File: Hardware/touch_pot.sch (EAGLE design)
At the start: 77 parts, among them CON1 SINGLE_PADSMD, CON10 SINGLE_PADSMD, CON11 SINGLE_PADSMD, CON12 SINGLE_PADSMD, CON13 SINGLE_PADSMD, CON14 SINGLE_PADSMD, CON15 SINGLE_PADSMD, CON16 SINGLE_PADSMD_R, CON17 SINGLE_PADSMD_R, CON18 SINGLE_PADSMD_R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

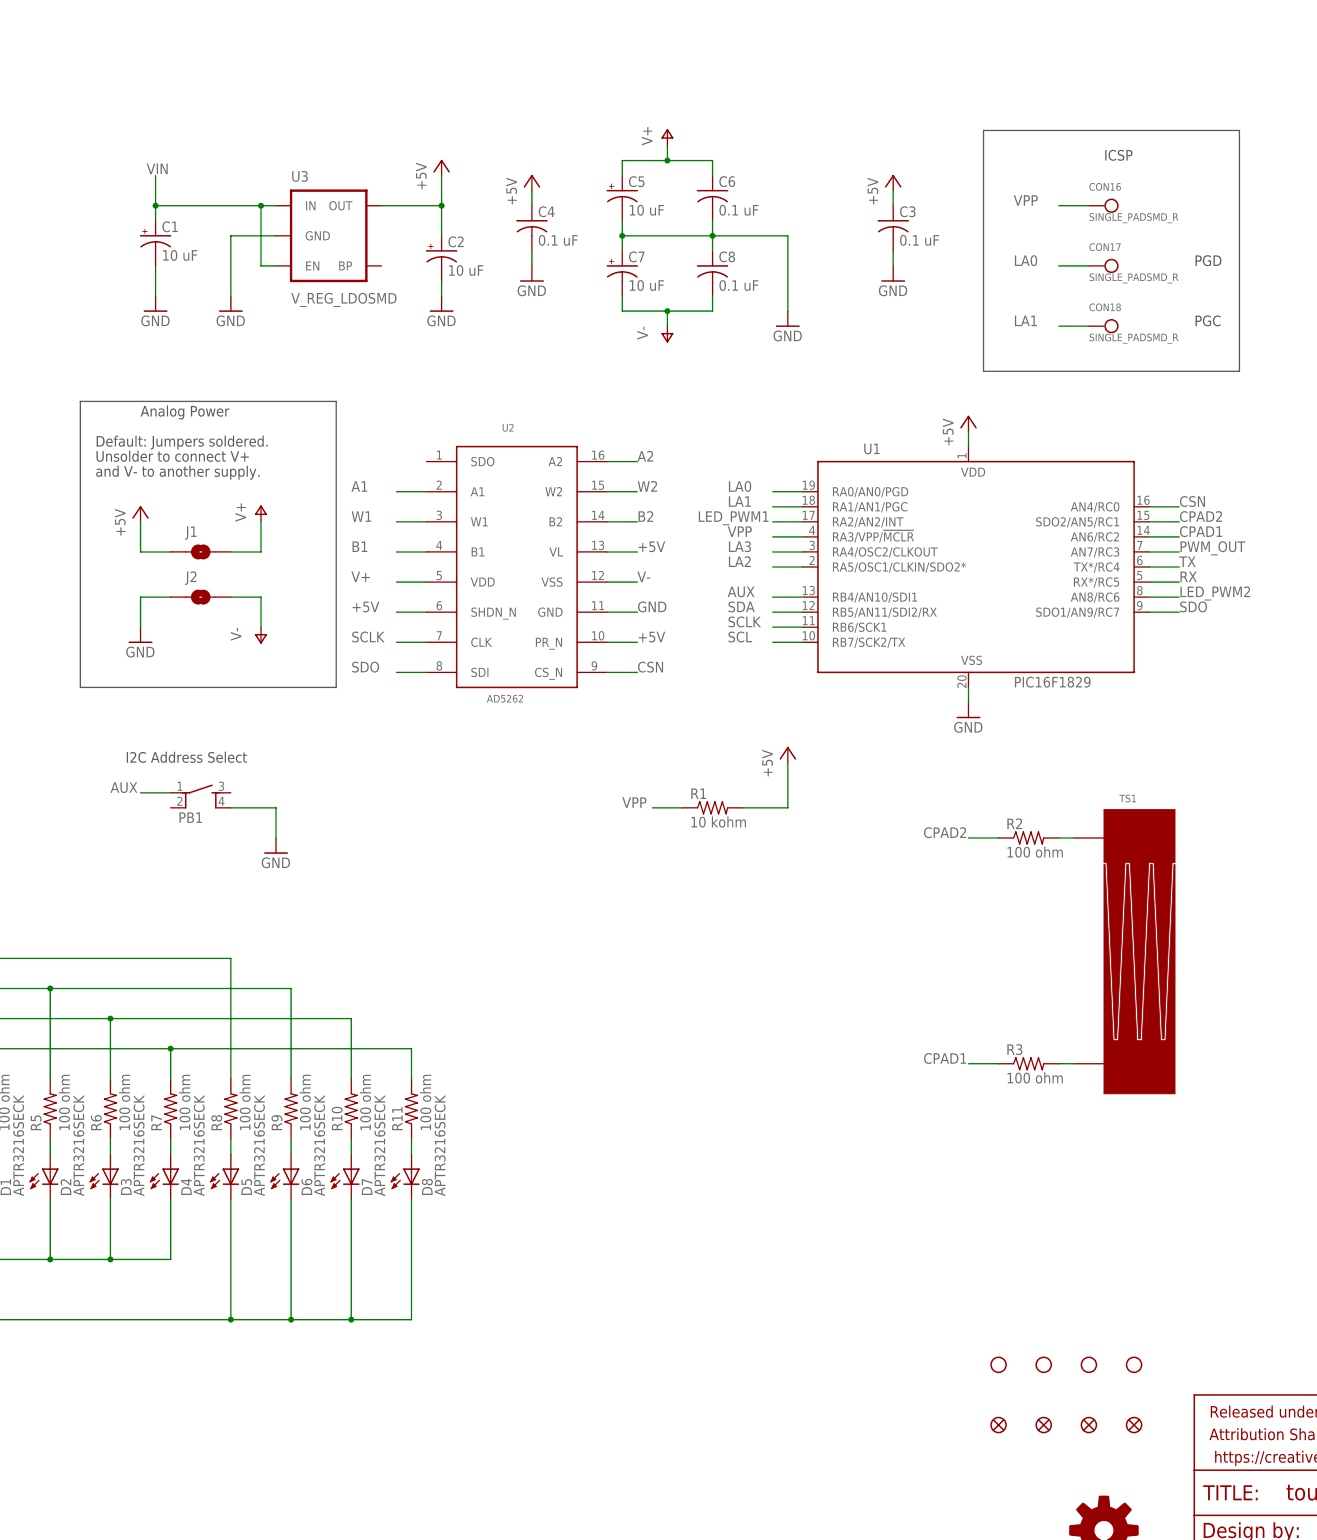
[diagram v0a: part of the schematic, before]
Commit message: 2nd Round of Protos
Added a few test points, moved a cap closer to analog IC, moved button
down to avoid touching resistors.
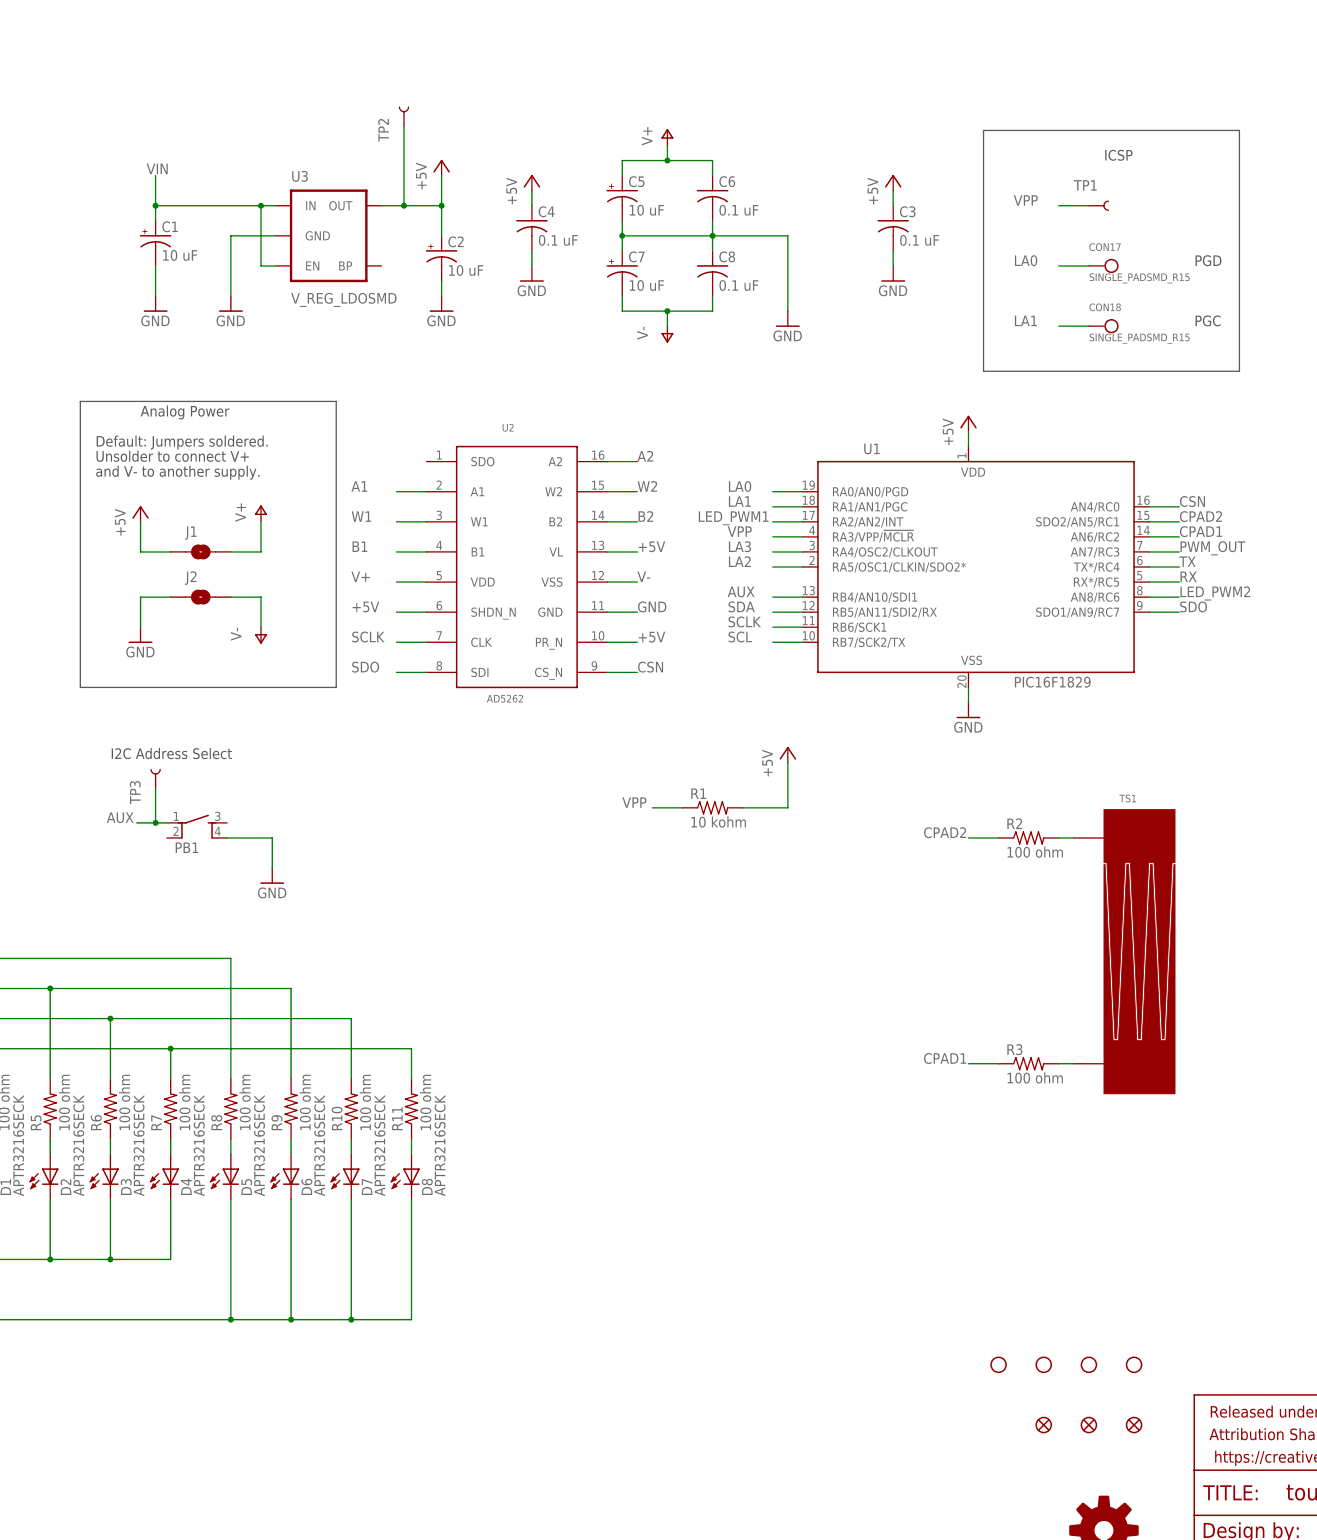
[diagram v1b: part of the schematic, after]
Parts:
- removed CON16: SINGLE_PADSMD_R, djd_eagle_library:SINGLE_PADSMD_R
- removed U$5: FIDUCIAL, djd_eagle_library:FIDUCIAL
- added TP1, TP2, TP3: TEST-POINT3X4, SparkFun-Passives:TEST-POINT3X4
- CON17, CON18: value SINGLE_PADSMD_R -> SINGLE_PADSMD_R15; device djd_eagle_library:SINGLE_PADSMD_R -> djd_eagle_library:SINGLE_PADSMD_R15
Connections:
- net +5V: now also TP2.1
- net AUX: now also TP3.1
- net VPP: now also TP1.1; no longer CON16.P$1
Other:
- moved on the sheet: PB1

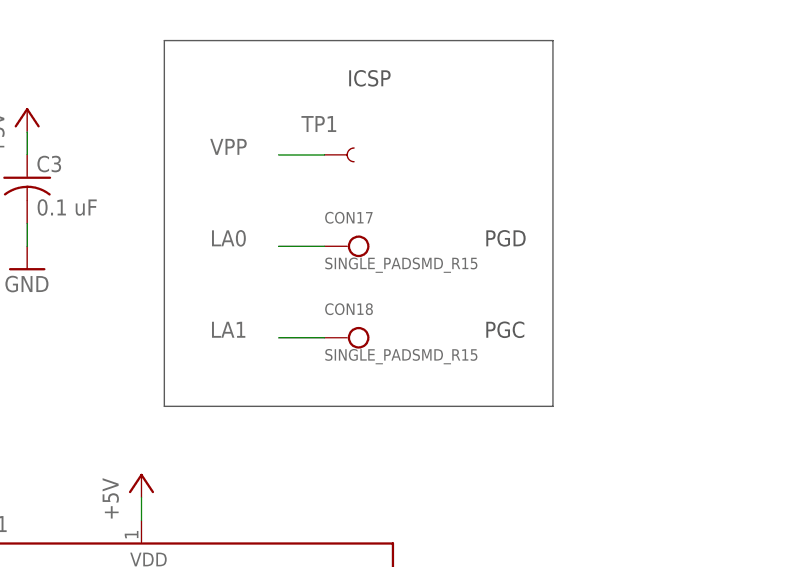
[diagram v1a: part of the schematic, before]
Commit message: Final commit before 2nd round of protos - 4 real
made all test points the same size, trace clean up, moved filtering cap
as close as possible.
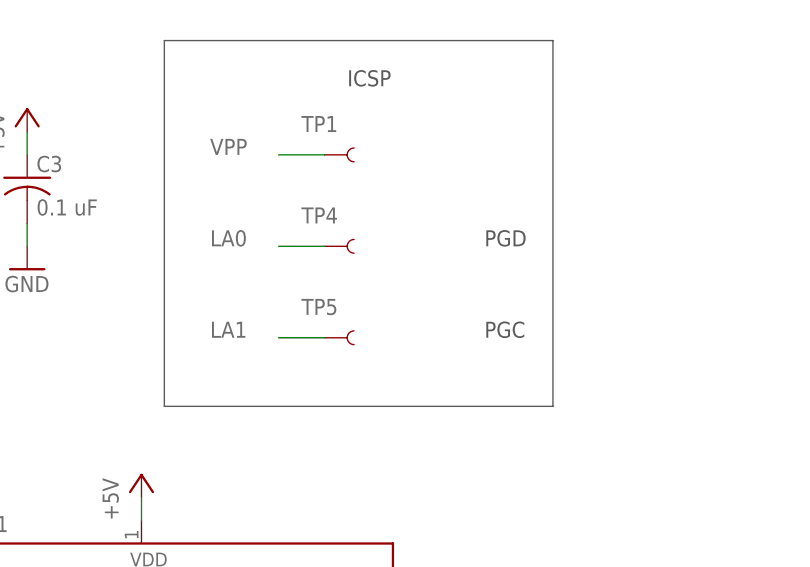
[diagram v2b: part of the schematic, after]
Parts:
- removed CON17, CON18: SINGLE_PADSMD_R15, djd_eagle_library:SINGLE_PADSMD_R15
- added TP4, TP5: TEST-POINT3X4, SparkFun-Passives:TEST-POINT3X4
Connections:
- net LA0: now also TP4.1; no longer CON17.P$1
- net LA1: now also TP5.1; no longer CON18.P$1
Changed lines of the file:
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@@
 <setting verticaltext="up"/>
 </settings>
-<grid distance="0.025" unitdist="inch" unit="inch" style="lines" multiple="1" display="no" altdistance="0.01" altunitdist="inch" altunit="inch"/>
+<grid distance="0.1" unitdist="inch" unit="inch" style="lines" multiple="1" display="no" altdistance="0.01" altunitdist="inch" altunit="inch"/>
 <layers>
-<layer number="1" name="Top" color="4" fill="1" visible="yes" active="no"/>
-<layer number="2" name="Route2" color="1" fill="3" visible="yes" active="no"/>
-<layer number="3" name="Route3" color="4" fill="3" visible="yes" active="no"/>
-<layer number="4" name="Route4" color="1" fill="4" visible="yes" active="no"/>
-<layer number="5" name="Route5" color="4" fill="4" visible="yes" active="no"/>
-<layer number="6" name="Route6" color="1" fill="8" visible="yes" active="no"/>
-<layer number="7" name="Route7" color="4" fill="8" visible="yes" active="no"/>
-<layer number="8" name="Route8" color="1" fill="2" visible="yes" active="no"/>
-<layer number="9" name="Route9" color="4" fill="2" visible="yes" active="no"/>
-<layer number="10" name="Route10" color="1" fill="7" visible="yes" active="no"/>
-<layer number="11" name="Route11" color="4" fill="7" visible="yes" active="no"/>
-<layer number="12" name="Route12" color="1" fill="5" visible="yes" active="no"/>
-<layer number="13" name="Route13" color="4" fill="5" visible="yes" active="no"/>
-<layer number="14" name="Route14" color="1" fill="6" visible="yes" active="no"/>
-<layer number="15" name="Route15" color="4" fill="6" visible="yes" active="no"/>
-<layer number="16" name="Bottom" color="1" fill="1" visible="yes" active="no"/>
-<layer number="17" name="Pads" color="2" fill="1" visible="yes" active="no"/>
-<layer number="18" name="Vias" color="2" fill="1" visible="yes" active="no"/>
-<layer number="19" name="Unrouted" color="6" fill="1" visible="yes" active="no"/>
-<layer number="20" name="Dimension" color="15" fill="1" visible="yes" active="no"/>
-<layer number="21" name="tPlace" color="16" fill="1" visible="yes" active="no"/>
-<layer number="22" name="bPlace" color="14" fill="1" visible="yes" active="no"/>
-<layer number="23" name="tOrigins" color="15" fill="1" visible="yes" active="no"/>
-<layer number="24" name="bOrigins" color="15" fill="1" visible="yes" active="no"/>
-<layer number="25" name="tNames" color="7" fill="1" visible="yes" active="no"/>
-<layer number="26" name="bNames" color="7" fill="1" visible="yes" active="no"/>
-<layer number="27" name="tValues" color="7" fill="1" visible="yes" active="no"/>
-<layer number="28" name="bValues" color="7" fill="1" visible="yes" active="no"/>
+<layer number="1" name="Top" color="4" fill="1" visible="no" active="no"/>
+<layer number="2" name="Route2" color="1" fill="3" visible="no" active="no"/>
+<layer number="3" name="Route3" color="4" fill="3" visible="no" active="no"/>
+<layer number="4" name="Route4" color="1" fill="4" visible="no" active="no"/>
+<layer number="5" name="Route5" color="4" fill="4" visible="no" active="no"/>
+<layer number="6" name="Route6" color="1" fill="8" visible="no" active="no"/>
+<layer number="7" name="Route7" color="4" fill="8" visible="no" active="no"/>
+<layer number="8" name="Route8" color="1" fill="2" visible="no" active="no"/>
+<layer number="9" name="Route9" color="4" fill="2" visible="no" active="no"/>
+<layer number="10" name="Route10" color="1" fill="7" visible="no" active="no"/>
+<layer number="11" name="Route11" color="4" fill="7" visible="no" active="no"/>
+<layer number="12" name="Route12" color="1" fill="5" visible="no" active="no"/>
+<layer number="13" name="Route13" color="4" fill="5" visible="no" active="no"/>
+<layer number="14" name="Route14" color="1" fill="6" visible="no" active="no"/>
+<layer number="15" name="Route15" color="4" fill="6" visible="no" active="no"/>
+<layer number="16" name="Bottom" color="1" fill="1" visible="no" active="no"/>
+<layer number="17" name="Pads" color="2" fill="1" visible="no" active="no"/>
+<layer number="18" name="Vias" color="2" fill="1" visible="no" active="no"/>
+<layer number="19" name="Unrouted" color="6" fill="1" visible="no" active="no"/>
+<layer number="20" name="Dimension" color="15" fill="1" visible="no" active="no"/>
+<layer number="21" name="tPlace" color="16" fill="1" visible="no" active="no"/>
+<layer number="22" name="bPlace" color="14" fill="1" visible="no" active="no"/>
+<layer number="23" name="tOrigins" color="15" fill="1" visible="no" active="no"/>
+<layer number="24" name="bOrigins" color="15" fill="1" visible="no" active="no"/>
+<layer number="25" name="tNames" color="7" fill="1" visible="no" active="no"/>
+<layer number="26" name="bNames" color="7" fill="1" visible="no" active="no"/>
+<layer number="27" name="tValues" color="7" fill="1" visible="no" active="no"/>
+<layer number="28" name="bValues" color="7" fill="1" visible="no" active="no"/>
 <layer number="29" name="tStop" color="7" fill="3" visible="no" active="no"/>
 <layer number="30" name="bStop" color="7" fill="6" visible="no" active="no"/>
@@
 <layer number="35" name="tGlue" color="7" fill="4" visible="no" active="no"/>
 <layer number="36" name="bGlue" color="7" fill="5" visible="no" active="no"/>
-<layer number="37" name="tTest" color="7" fill="1" visible="yes" active="no"/>
-<layer number="38" name="bTest" color="7" fill="1" visible="yes" active="no"/>
+<layer number="37" name="tTest" color="7" fill="1" visible="no" active="no"/>
+<layer number="38" name="bTest" color="7" fill="1" visible="no" active="no"/>
 <layer number="39" name="tKeepout" color="4" fill="11" visible="no" active="no"/>
 <layer number="40" name="bKeepout" color="1" fill="11" visible="no" active="no"/>
@@
 <layer number="44" name="Drills" color="7" fill="1" visible="no" active="no"/>
 <layer number="45" name="Holes" color="7" fill="1" visible="no" active="no"/>
-<layer number="46" name="Milling" color="3" fill="1" visible="yes" active="no"/>
-<layer number="47" name="Measures" color="7" fill="1" visible="yes" active="no"/>
-<layer number="48" name="Document" color="7" fill="1" visible="yes" active="no"/>
-<layer number="49" name="Reference" color="7" fill="1" visible="yes" active="no"/>
-<layer number="50" name="dxf" color="7" fill="1" visible="yes" active="no"/>
-<layer number="51" name="tDocu" color="6" fill="1" visible="yes" active="no"/>
-<layer number="52" name="bDocu" color="7" fill="1" visible="yes" active="no"/>
-<layer number="53" name="tGND_GNDA" color="7" fill="9" visible="yes" active="no"/>
-<layer number="54" name="bGND_GNDA" color="1" fill="9" visible="yes" active="no"/>
-<layer number="56" name="wert" color="7" fill="1" visible="yes" active="no"/>
-<layer number="57" name="tCAD" color="7" fill="1" visible="yes" active="no"/>
+<layer number="46" name="Milling" color="3" fill="1" visible="no" active="no"/>
+<layer number="47" name="Measures" color="7" fill="1" visible="no" active="no"/>
+<layer number="48" name="Document" color="7" fill="1" visible="no" active="no"/>
+<layer number="49" name="Reference" color="7" fill="1" visible="no" active="no"/>
+<layer number="50" name="dxf" color="7" fill="1" visible="no" active="no"/>
+<layer number="51" name="tDocu" color="6" fill="1" visible="no" active="no"/>
+<layer number="52" name="bDocu" color="7" fill="1" visible="no" active="no"/>
+<layer number="53" name="tGND_GNDA" color="7" fill="9" visible="no" active="no"/>
+<layer number="54" name="bGND_GNDA" color="1" fill="9" visible="no" active="no"/>
+<layer number="56" name="wert" color="7" fill="1" visible="no" active="no"/>
+<layer number="57" name="tCAD" color="7" fill="1" visible="no" active="no"/>
 <layer number="91" name="Nets" color="2" fill="1" visible="yes" active="yes"/>
 <layer number="92" name="Busses" color="1" fill="1" visible="yes" active="yes"/>
@@
 <part name="R1" library="djd_eagle_library" deviceset="R-US" device="SMT0603" value="10 kohm"/>
 <part name="P+6" library="supply1" deviceset="+5V" device=""/>
-<part name="CON17" library="djd_eagle_library" deviceset="SINGLE_PAD" device="SMD_R15" value="SINGLE_PADSMD_R15"/>
-<part name="CON18" library="djd_eagle_library" deviceset="SINGLE_PAD" device="SMD_R15" value="SINGLE_PADSMD_R15"/>
 <part name="GND6" library="supply1" deviceset="GND" device=""/>
 <part name="R4" library="djd_eagle_library" deviceset="R-US" device="SMT0603" value="100 ohm"/>
@@
 <part name="TP3" library="SparkFun-Passives" deviceset="TEST-POINT" device="3X4" value=""/>
 <part name="TP1" library="SparkFun-Passives" deviceset="TEST-POINT" device="3X4" value=""/>
+<part name="TP4" library="SparkFun-Passives" deviceset="TEST-POINT" device="3X4" value=""/>
+<part name="TP5" library="SparkFun-Passives" deviceset="TEST-POINT" device="3X4" value=""/>
 </parts>
 <sheets>
@@
 <instance part="R1" gate="G$1" x="248.92" y="134.62"/>
 <instance part="P+6" gate="1" x="261.62" y="144.78"/>
-<instance part="CON17" gate="G$1" x="314.96" y="226.06"/>
-<instance part="CON18" gate="G$1" x="314.96" y="215.9"/>
 <instance part="GND6" gate="1" x="174.625" y="121.92"/>
 <instance part="R4" gate="G$1" x="127" y="83.82" rot="R90"/>
@@
 <instance part="TP3" gate="G$1" x="154.94" y="137.795" rot="R90"/>
 <instance part="TP1" gate="G$1" x="312.42" y="236.22"/>
+<instance part="TP4" gate="G$1" x="312.42" y="226.06"/>
+<instance part="TP5" gate="G$1" x="312.42" y="215.9"/>
 </instances>
 <busses>
@@
 <wire x1="307.34" y1="215.9" x2="312.42" y2="215.9" width="0.1524" layer="91"/>
 <label x="299.72" y="215.9" size="1.778" layer="95"/>
-<pinref part="CON18" gate="G$1" pin="P$1"/>
+<pinref part="TP5" gate="G$1" pin="1"/>
 </segment>
 </net>
@@
 <wire x1="307.34" y1="226.06" x2="312.42" y2="226.06" width="0.1524" layer="91"/>
 <label x="299.72" y="226.06" size="1.778" layer="95"/>
-<pinref part="CON17" gate="G$1" pin="P$1"/>
-</segment>
-</net>
+<pinref part="TP4" gate="G$1" pin="1"/>
+</segment>
+</net>

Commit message: Schematic Cleanup
added flags, added I2C and VIN Info, general cleanup
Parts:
- added U$5: SFE_LOGO_NAME_WEB, SparkFun-Aesthetics:SFE_LOGO_NAME_WEB
- U3: value V_REG_LDOSMD -> 5V_REG_LDOSMD
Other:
- note added: "11"
- note added: "Analog IC"
- note added: "DEFAULT I2C ADDRESS: 0x08"
- note added: "Joel Bartlett"
- note added: "Vin = 5-12V"
- note removed: "10"
- moved on the sheet: C1, C2, C3, C4, C5, C6, C7, C8, CON1, CON10, CON11, CON12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
